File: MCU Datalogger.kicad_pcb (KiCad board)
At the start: 2 copper layers, 29 parts, among them J1 Conn_01x04_Pin, J2 Conn_01x09_Pin, J3 Conn_01x04_Pin, J4 Conn_02x03_Odd_Even, U1 24LC1025, U2 DS1337S_, U3 24LC1025, U4 ATMEGA328P-AU, Y1 32.728KHz, Y2 16MHz

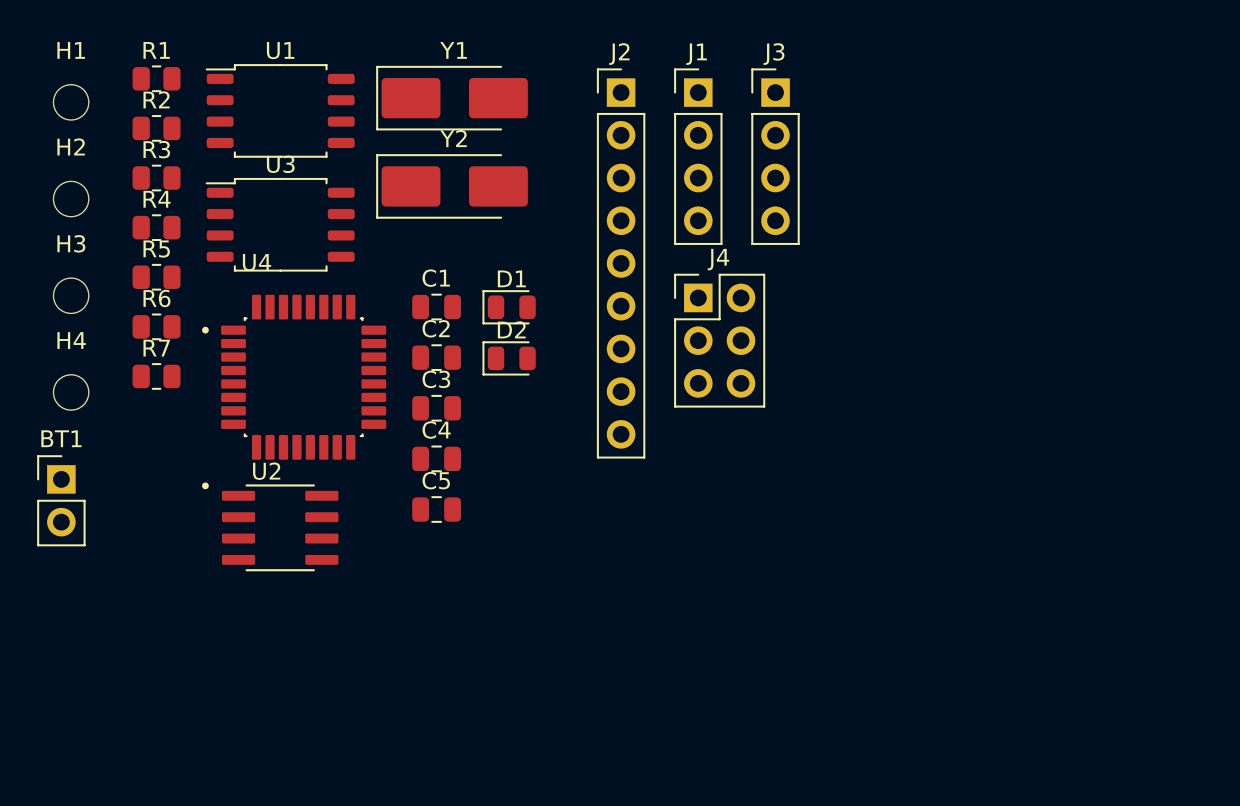
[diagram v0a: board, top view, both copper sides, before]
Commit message: completed placement of footprints
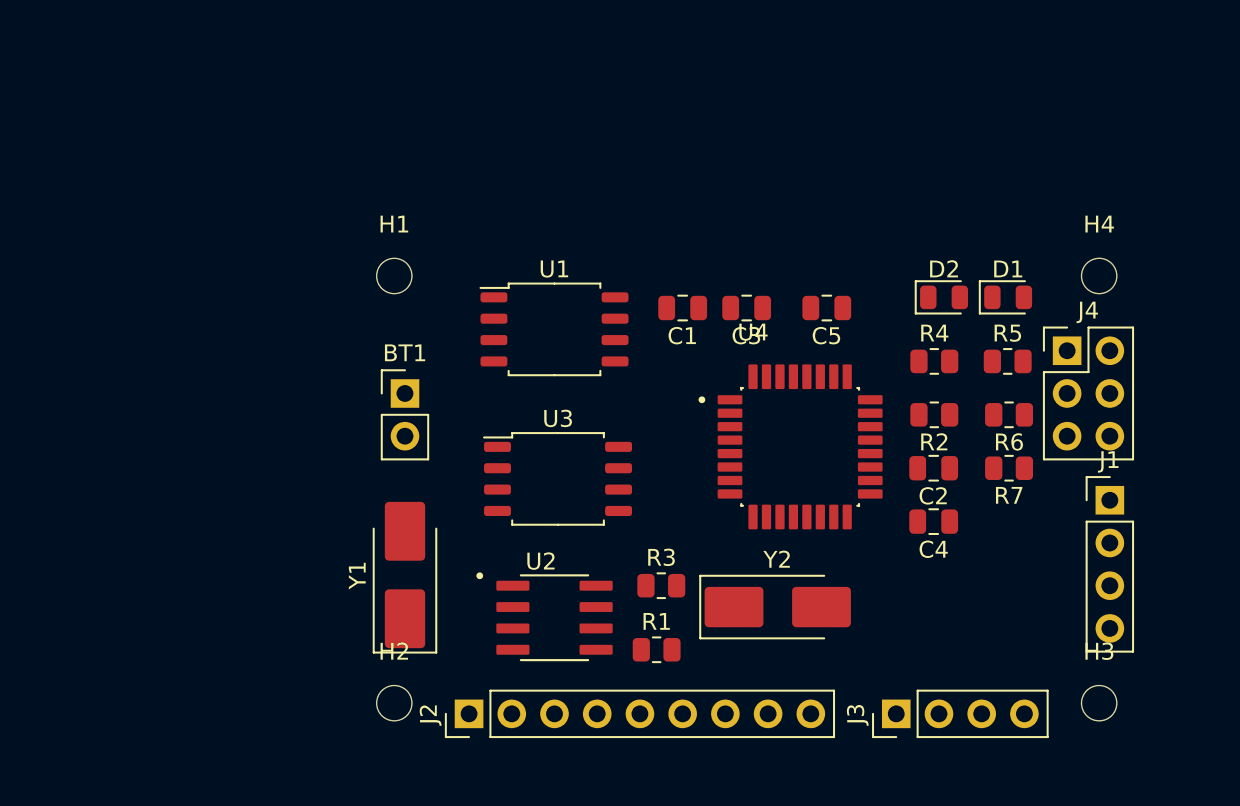
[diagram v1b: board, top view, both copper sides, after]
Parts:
- moved H3 65.8 mm to (171.4, 99.1)
- moved H4 61.5 mm to (171.4, 73.7)
- moved R7 51.0 mm to (166.1, 85.1), turned to 180 degrees
- moved R6 51.0 mm to (166.1, 81.9), turned to 180 degrees
- moved R5 50.9 mm to (166.0, 78.7)
- moved R2 49.3 mm to (161.6, 81.9), turned to 180 degrees
- moved R4 46.9 mm to (161.6, 78.7)
- moved R1 45.1 mm to (145.1, 95.9)
- moved R3 38.6 mm to (145.4, 92.1)
- moved J2 38.0 mm to (134.0, 99.7), turned to 90 degrees
- moved J3 37.6 mm to (159.4, 99.7), turned to 90 degrees
- moved H2 35.6 mm to (129.5, 99.1)
- moved J1 34.4 mm to (172.1, 87.0)
- moved Y2 31.5 mm to (152.3, 93.3)
- moved C2 30.3 mm to (161.6, 85.1), turned to 180 degrees
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
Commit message: general layout completed ,GND and VCC left
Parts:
- moved U3 8.60 mm to (139.4, 77.1)
- moved R1 8.27 mm to (136.9, 95.5)
- moved U1 7.39 mm to (139.7, 84.2)
- moved R7 6.53 mm to (162.1, 79.9), turned to 0 degrees
- moved C2 6.48 mm to (160.3, 91.4)
- moved C4 5.86 mm to (160.3, 94.0), turned to 0 degrees
- moved R3 5.37 mm to (141.3, 95.5), turned to 180 degrees
- moved R4 4.85 mm to (162.2, 83.5), turned to 180 degrees
- moved R2 4.82 mm to (162.3, 86.7)
- moved H3 3.95 mm to (175.1, 100.5)
- moved H4 3.69 mm to (175.1, 73.8)
- moved U2 3.36 mm to (139.9, 90.7)
- moved Y1 2.65 mm to (132.1, 89.6)
- moved BT1 1.91 mm to (132.1, 80.6)
- moved R6 1.72 mm to (166.6, 83.5), turned to 0 degrees
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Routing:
- net /VCC: track 0.00 -> 93.3 mm, vias 0 -> 3
- net /SCK: track 0.00 -> 93.1 mm, vias 0 -> 3
- net Net-(BT1-+): track 0.00 -> 73.4 mm, vias 0 -> 7
- net /SDA: track 0.00 -> 58.2 mm, vias 0 -> 2
- net GND: track 0.00 -> 37.7 mm, vias 0 -> 6
- net /D2: track 0.00 -> 28.7 mm, vias 0 -> 1
- net /TX: track 0.00 -> 25.9 mm, vias 0 -> 1
- net /D3: track 0.00 -> 24.9 mm, vias 0 -> 1
- net /RX: track 0.00 -> 23.5 mm, vias 0 -> 1
- net Net-(U4-PB6): track 0.00 -> 23.0 mm, vias 0 -> 2
- net /MOSI: track 0.00 -> 22.6 mm
- net /D4: track 0.00 -> 22.3 mm, vias 0 -> 1
- net /RESET: track 0.00 -> 19.8 mm, vias 0 -> 2
- net /MISO: track 0.00 -> 18.6 mm, vias 0 -> 1
- net /D5: track 0.00 -> 15.0 mm, vias 0 -> 1
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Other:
- board outline added: 51 x 31.9 mm
